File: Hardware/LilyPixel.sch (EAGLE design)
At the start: 12 parts

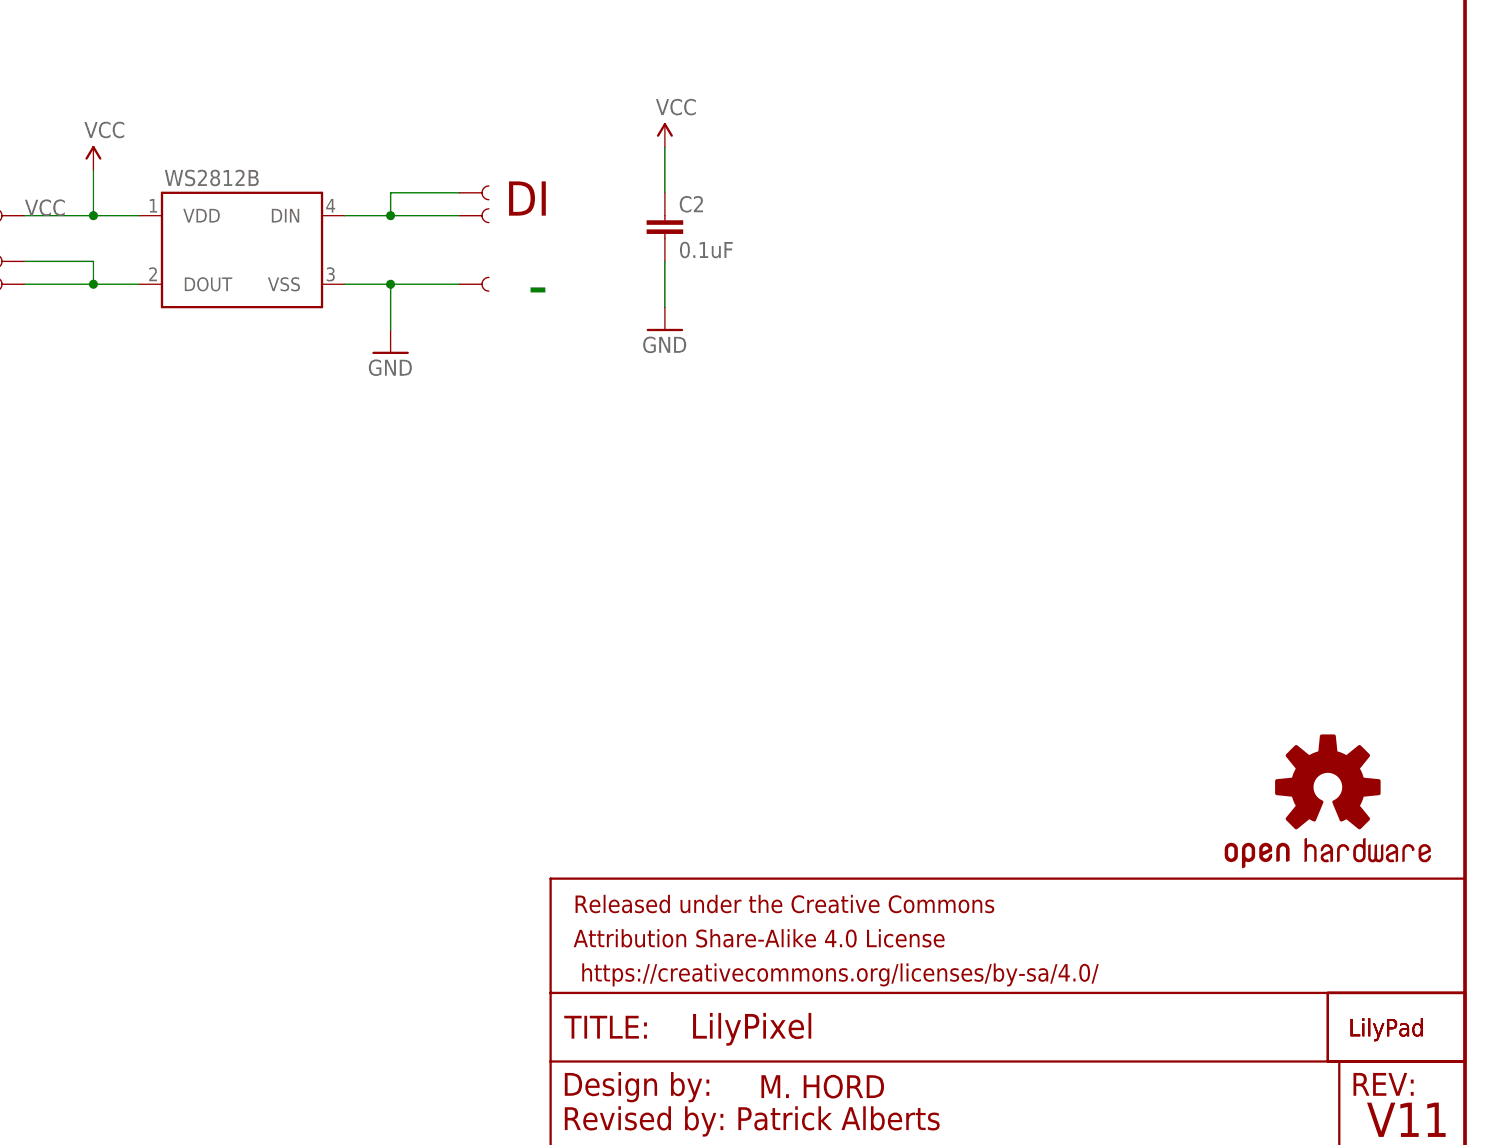
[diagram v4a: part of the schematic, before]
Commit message: Fixed qc checklist problems
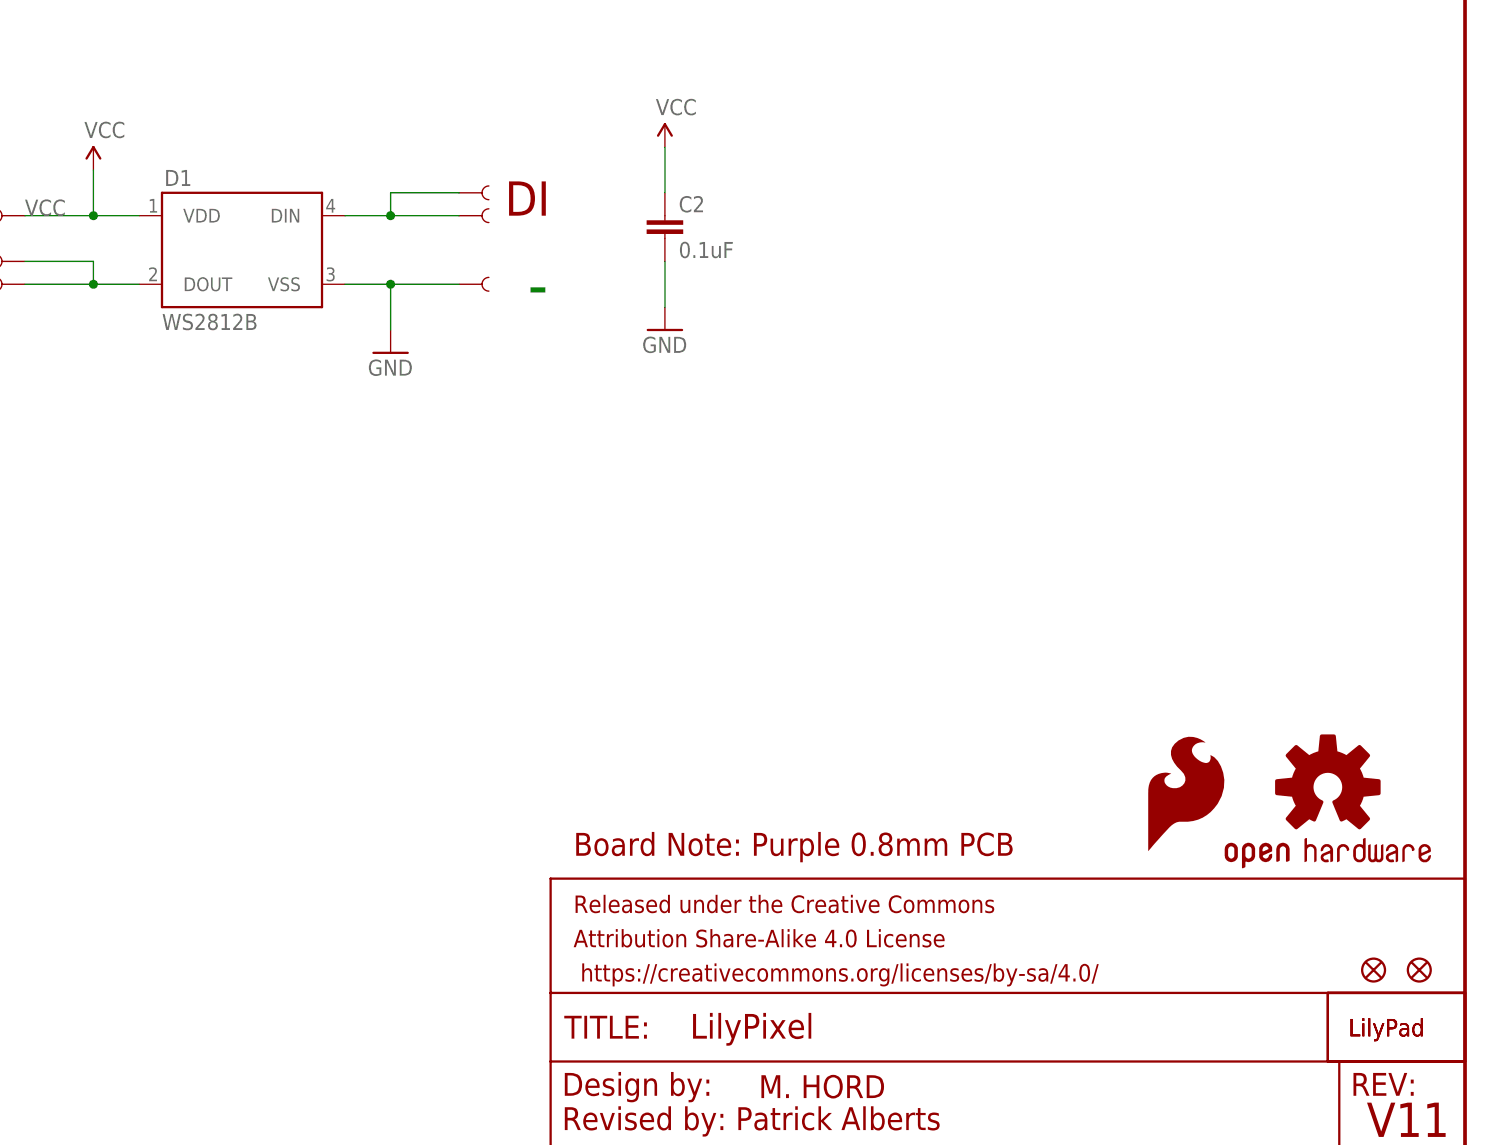
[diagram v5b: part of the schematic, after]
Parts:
- added FID1, FID2: FIDUCIALUFIDUCIAL, SparkFun-Aesthetics:FIDUCIALUFIDUCIAL
- added LOGO2: SFE_LOGO_FLAME.1_INCH, SparkFun-Aesthetics:SFE_LOGO_FLAME.1_INCH
- D1: value (none) -> WS2812B
- renumbered WS2812B to D1
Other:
- note added: "Board Note: Purple 0.8mm PCB"
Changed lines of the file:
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@@
 <layer number="111" name="LPC17xx" color="7" fill="1" visible="yes" active="yes"/>
 <layer number="112" name="tSilk" color="7" fill="1" visible="yes" active="yes"/>
+<layer number="113" name="IDFDebug" color="4" fill="1" visible="yes" active="yes"/>
 <layer number="116" name="Patch_BOT" color="9" fill="4" visible="yes" active="yes"/>
 <layer number="121" name="_tsilk" color="7" fill="1" visible="yes" active="yes"/>
@@
 <part name="FRAME1" library="SparkFun-Aesthetics" deviceset="FRAME-LETTER" device=""/>
 <part name="U$1" library="LilyPad-Wearables" deviceset="LOGO-LP" device="LP"/>
-<part name="WS2812B" library="SparkFun-LED" deviceset="WS2812B" device=""/>
+<part name="D1" library="SparkFun-LED" deviceset="WS2812B" device="" value="WS2812B"/>
 <part name="JP4" library="LilyPad-Wearables" deviceset="SEWTAP" device="6"/>
 <part name="JP5" library="LilyPad-Wearables" deviceset="SEWTAP" device="6"/>
@@
 <part name="GND3" library="SparkFun" deviceset="GND" device=""/>
 <part name="LOGO1" library="SparkFun-Aesthetics" deviceset="OSHW-LOGO" device="S"/>
+<part name="LOGO2" library="SparkFun-Aesthetics" deviceset="SFE_LOGO_FLAME" device=".1_INCH"/>
+<part name="FID1" library="SparkFun-Aesthetics" deviceset="FIDUCIAL" device="UFIDUCIAL"/>
+<part name="FID2" library="SparkFun-Aesthetics" deviceset="FIDUCIAL" device="UFIDUCIAL"/>
 </parts>
 <sheets>
@@
 <text x="148.59" y="7.62" size="2.54" layer="94">Revised by: Patrick Alberts</text>
 <text x="45.72" y="109.22" size="1.778" layer="97">VCC: 3.5v to 5.3v</text>
+<text x="149.86" y="38.1" size="2.54" layer="94">Board Note: Purple 0.8mm PCB</text>
 </plain>
 <instances>
@@
 <instance part="FRAME1" gate="G$2" x="147.32" y="0"/>
 <instance part="U$1" gate="G$1" x="236.22" y="17.78"/>
-<instance part="WS2812B" gate="G$1" x="106.68" y="104.14"/>
+<instance part="D1" gate="G$1" x="106.68" y="104.14"/>
 <instance part="JP4" gate="G$1" x="86.36" y="109.22" rot="R180"/>
 <instance part="JP5" gate="G$1" x="139.7" y="109.22"/>
@@
 <instance part="GND3" gate="1" x="160.02" y="96.52"/>
 <instance part="LOGO1" gate="G$1" x="233.68" y="45.72"/>
+<instance part="LOGO2" gate="G$1" x="213.36" y="38.1"/>
+<instance part="FID1" gate="G$1" x="238.76" y="25.4"/>
+<instance part="FID2" gate="G$1" x="243.84" y="25.4"/>
 </instances>
 <busses>
@@
 <wire x1="96.52" y1="109.22" x2="101.6" y2="109.22" width="0.1524" layer="91"/>
 <label x="88.9" y="109.22" size="1.778" layer="95"/>
-<pinref part="WS2812B" gate="G$1" pin="VDD"/>
+<pinref part="D1" gate="G$1" pin="VDD"/>
 <pinref part="JP4" gate="G$1" pin="1"/>
 <wire x1="88.9" y1="109.22" x2="96.52" y2="109.22" width="0.1524" layer="91"/>
@@
 </segment>
 <segment>
-<pinref part="WS2812B" gate="G$1" pin="VSS"/>
+<pinref part="D1" gate="G$1" pin="VSS"/>
 <wire x1="124.46" y1="101.6" x2="129.54" y2="101.6" width="0.1524" layer="91"/>
 <wire x1="129.54" y1="101.6" x2="129.54" y2="96.52" width="0.1524" layer="91"/>
@@
 <wire x1="137.16" y1="109.22" x2="129.54" y2="109.22" width="0.1524" layer="91"/>
 <junction x="129.54" y="109.22"/>
-<pinref part="WS2812B" gate="G$1" pin="DIN"/>
+<pinref part="D1" gate="G$1" pin="DIN"/>
 <pinref part="JP6" gate="G$1" pin="1"/>
 <wire x1="137.16" y1="111.76" x2="129.54" y2="111.76" width="0.1524" layer="91"/>
@@
 <pinref part="JP2" gate="G$1" pin="1"/>
 <wire x1="88.9" y1="104.14" x2="96.52" y2="104.14" width="0.1524" layer="91"/>
-<pinref part="WS2812B" gate="G$1" pin="DOUT"/>
+<pinref part="D1" gate="G$1" pin="DOUT"/>
 <pinref part="JP1" gate="G$1" pin="1"/>
 <wire x1="88.9" y1="101.6" x2="96.52" y2="101.6" width="0.1524" layer="91"/>
